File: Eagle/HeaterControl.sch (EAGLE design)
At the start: 38 parts, among them Q1 P-FET

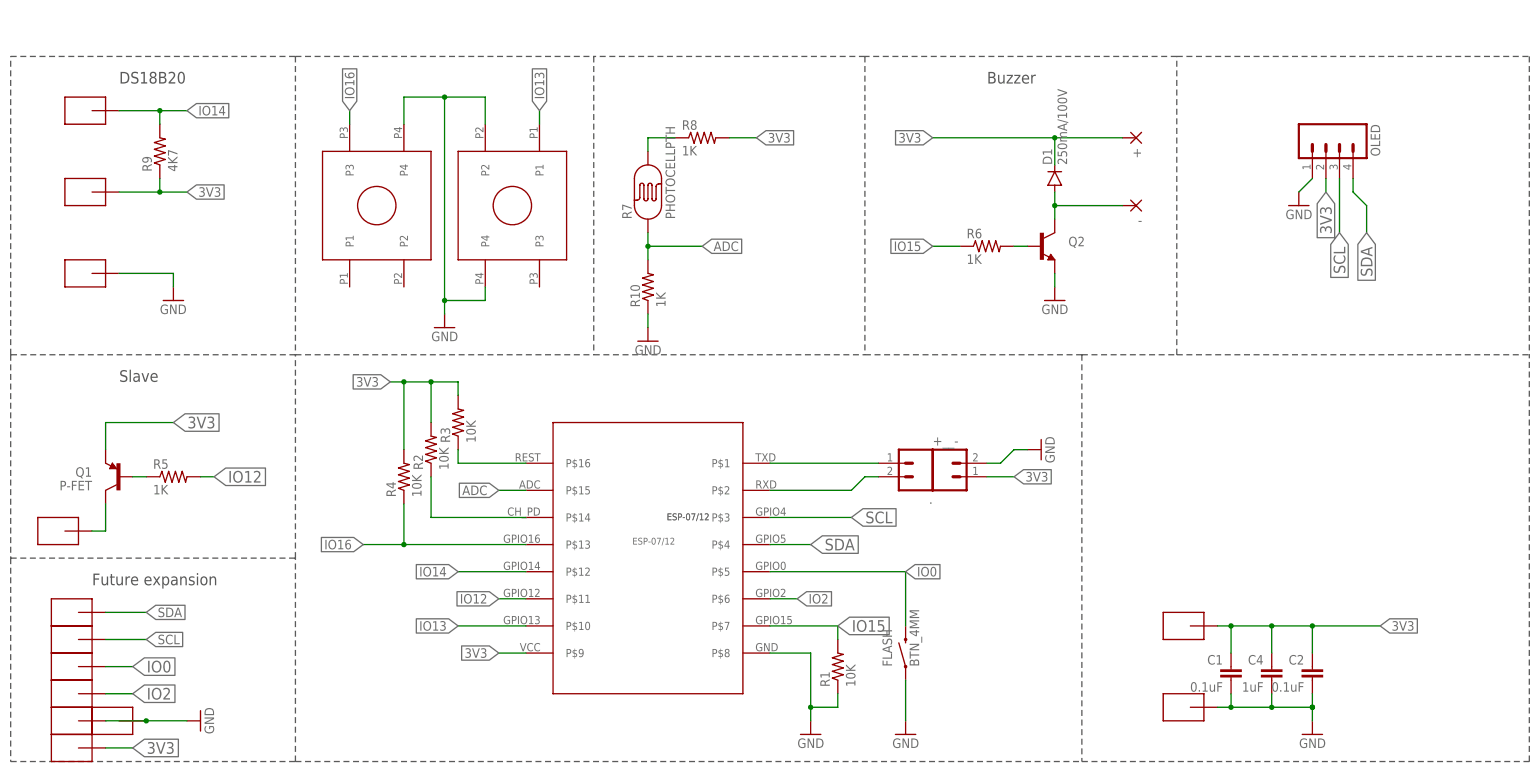
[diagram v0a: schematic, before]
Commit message: Added top buttons
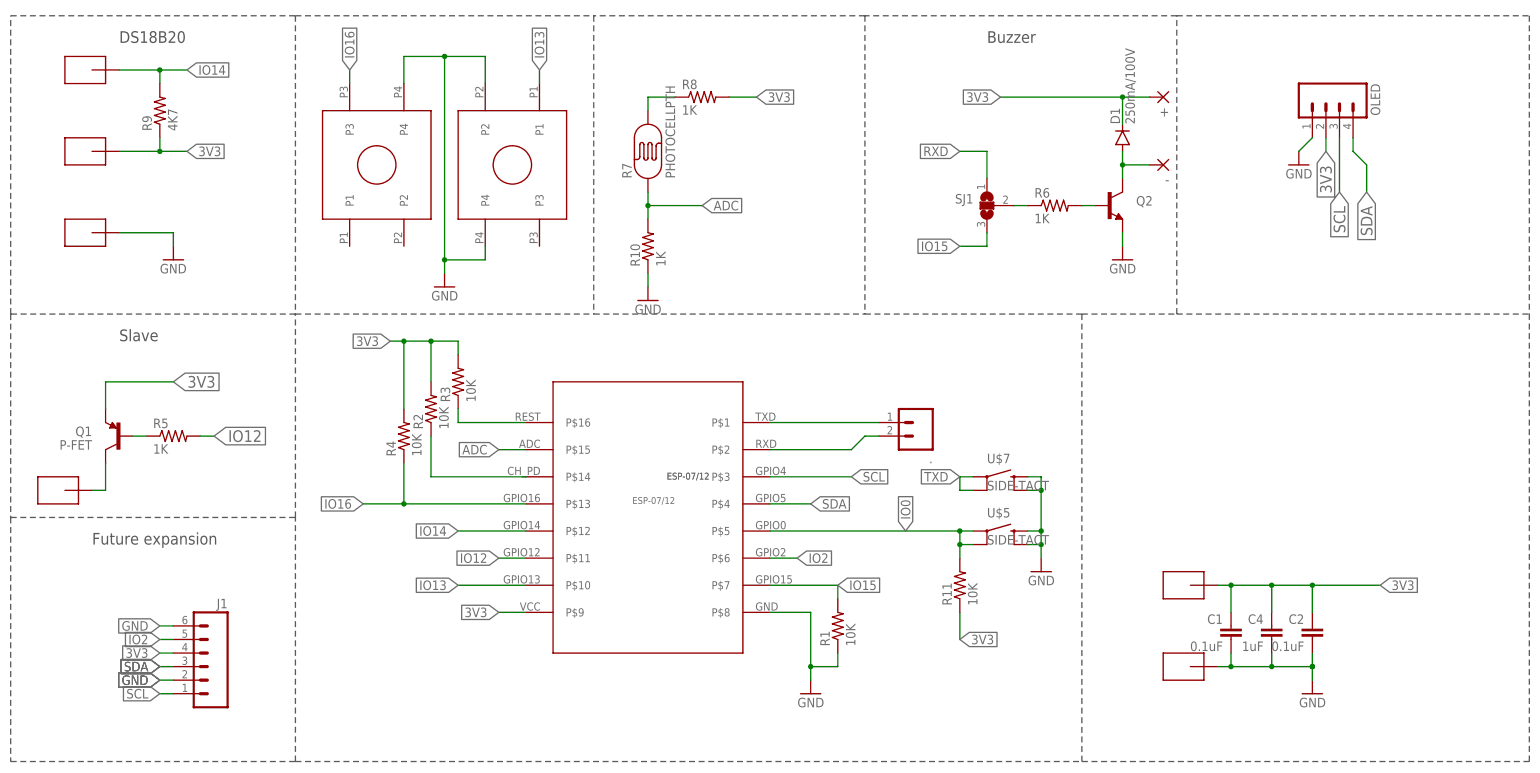
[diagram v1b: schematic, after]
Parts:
- removed +__-: (no value), SparkFun-Connectors:M02PTH
- removed FLASH: BTN_4MM, CuriousTech:BTN_4MM
- removed U$12, U$13, U$14, U$15, U$16, U$4, U$9: SMD-PAD1, CuriousTech:SMD-PAD1
- added J1: (no value), SparkFun-Connectors:M06SILK_FEMALE_PTH
- added R11: 10K, SparkFun-Resistors:RESISTOR0805-RES
- added SJ1: (no value), jumper:SJ2W
- added U$5, U$7: SIDE-TACT, CuriousTech:SIDE-TACT
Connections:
- new net N$8: R6.1, SJ1.2
- net 3V3: now also J1.4, R11.1; no longer +__-.1, U$9.P$1
- net GND: now also J1.2, J1.6, U$5.2, U$5.4, U$7.2, U$7.4; no longer +__-.2, FLASH.1, U$13.P$1, U$4.P$1
- net IO0: now also R11.2, U$5.1, U$5.3; no longer FLASH.2, U$14.P$1
- net IO15: now also SJ1.3; no longer R6.1
- net IO2: now also J1.5; no longer U$12.P$1
- net RXD: now also SJ1.1
- net SCL: now also J1.1; no longer U$15.P$1
- net SDA: now also J1.3; no longer U$16.P$1
- net TXD: now also U$7.1, U$7.3
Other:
- moved on the sheet: +, -, ., C1, C2, C4, D1, OLED, Q1, Q2, R1, R10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
